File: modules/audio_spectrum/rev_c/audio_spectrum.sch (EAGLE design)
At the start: 97 parts, among them J1 MODULE_GENERIC_DEBUG, J2 AUDIO-JACK-VERTICAL, J7 TC2030-JLINK-L, P1 4k-200k, P2 4k-200k, Q1 NX3008PBK, Q2 NX3008PBK, U1 AT45DB641EUDFN, U2 MSGEQ7, U3 MSGEQ7, U5 OPA344, U6 OPA344, U7 TLV62130, U8 MP23AB02B, X1 16MHz

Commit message: added amplifier for sam4l adc, routed pcb
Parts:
- added C31, C32: 1.2nF, passives:CAPACITOR0603_CAP
- added R28, R31: 1.5k, passives:RESISTOR0603_RES
- added R29, R30: 19k, passives:RESISTOR0603_RES
- added U4, U9: OPA344, SparkFun-AnalogIC:OPA344
- renumbered U$1 to U100
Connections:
- removed net N$31: U100.PA06
- new net N$24: TP8.TESTPOINT, U100.PB01
- new net N$26: C31.2, R28.2, R29.1, U4.-IN
- new net N$8: C32.2, R30.1, R31.2, U9.-IN
- new net N87: C6.1, C7.2, P2.W, R17.2, R31.1, TP10.TESTPOINT, U6.OUT
- new net N90: C5.1, C8.2, P1.W, R14.2, R28.1, TP9.TESTPOINT, U5.OUT
- net !FLASH_CS: now also U1.!CS, U100.PA15; no longer U100.PB06
- net !FLASH_RESET: now also U1.!RESET
- net 3V3: now also U1.!WP, U1.VCC
- net ADC_IN_EXTRN: now also C32.1, R30.2, U9.OUT; no longer C6.1, C7.2, P2.W, R17.2, TP10.TESTPOINT, U6.OUT
- net ADC_IN_MEMS: now also C31.1, R29.2, U4.OUT; no longer C5.1, C8.2, P1.W, R14.2, TP9.TESTPOINT, U5.OUT
- net DBG_RX: now also U100.PA11; no longer U100.PB01
- net DBG_TX: now also U100.PA12; no longer U100.PB00
- net FLASH_SCLK: now also U1.SCK
- net FLASH_SI: now also U1.SI
- net FLASH_SO: now also U1.SO
- net GND: now also U1.GND, U4.+IN, U4.V-, U9.+IN, U9.V-
- net LEDG1: now also U100.PB06; no longer U100.PA16
- net LEDG2: now also U100.PB04; no longer U100.PA14
- net LEDR1: now also U100.PB07; no longer U100.PA17
- net LEDR2: now also U100.PB05; no longer U100.PA15
- net N$22: now also TP7.TESTPOINT, U100.PB00; no longer U1.!WP
- net SPEC2_GATED: now also U9.V+
- net SPEC2_STROBE: now also U100.PA06; no longer U100.PA09
- net SPEC_GATED: now also U4.V+
- net SPEC_POWER: no longer TP8.TESTPOINT, U100.PA12
- net SPEC_RESET: no longer TP7.TESTPOINT, U100.PA11
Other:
- note removed: "Controller"
- moved on the sheet: C11, C12, C13, C14, C21, C22, C23, C25, C26, C29, C3, C30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

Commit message: added digikey part attribute for all parts
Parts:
- C10: DIGIKEY (none) -> 490-1503-1-ND
- C11, C12, C14, C15: DIGIKEY (none) -> 490-1532-1-ND
- C21, C22, C23: DIGIKEY (none) -> 490-1536-1-ND
- C25, C26: DIGIKEY (none) -> 490-3297-1-ND
- C27: DIGIKEY (none) -> 490-6405-1-ND
- C28: DIGIKEY (none) -> 490-13241-1-ND
- C29, C30: DIGIKEY (none) -> 490-1440-1-ND
- C3, C4: DIGIKEY (none) -> 490-1415-1-ND
- C31, C32: DIGIKEY (none) -> 490-1304-1-ND
- C5, C6: DIGIKEY (none) -> 490-1427-1-ND
- C7, C8, C9: DIGIKEY (none) -> 490-1494-1-ND
- LED1, LED3: DIGIKEY (none) -> 160-1446-1-ND
- LED2, LED4: DIGIKEY (none) -> 160-1447-1-ND
- R10, R11, R12, R13: DIGIKEY (none) -> RHM20KCGCT-ND
- R14: DIGIKEY (none) -> RHM60.4KCLCT-ND
- R17, R18, R23, R24: DIGIKEY (none) -> RHM100KCGCT-ND
- R19, R20: DIGIKEY (none) -> RHM200KCFCT-ND
- R21: DIGIKEY (none) -> RHM240KCFCT-ND
- R22: DIGIKEY (none) -> RHM750KCFCT-ND
- R26, R27, R8, R9: DIGIKEY (none) -> RHM10.0KHCT-ND
- R28, R31, R5, R6: DIGIKEY (none) -> RHM1.5KCGCT-ND
- R29, R30: DIGIKEY (none) -> RHM19.1KCFCT-ND
- U4, U5, U6, U9: DIGIKEY (none) -> OPA344NACT-ND

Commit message: update to fix comments
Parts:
- removed TP11, TP12, TP13, TP14, TP15, TP16: TEST_POINT_0.040IN, headers:TEST_POINT_0.040IN
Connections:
- net GND: no longer TP11.TESTPOINT
- net MOD_IN: no longer TP14.TESTPOINT
- net MOD_OUT: no longer TP15.TESTPOINT
- net PPS: no longer TP16.TESTPOINT
- net SCL: no longer TP12.TESTPOINT
- net SDA: no longer TP13.TESTPOINT
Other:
- note added: "Gain set to 12.59 (22dB) matches MSGEQ7 22 dB internal amp"

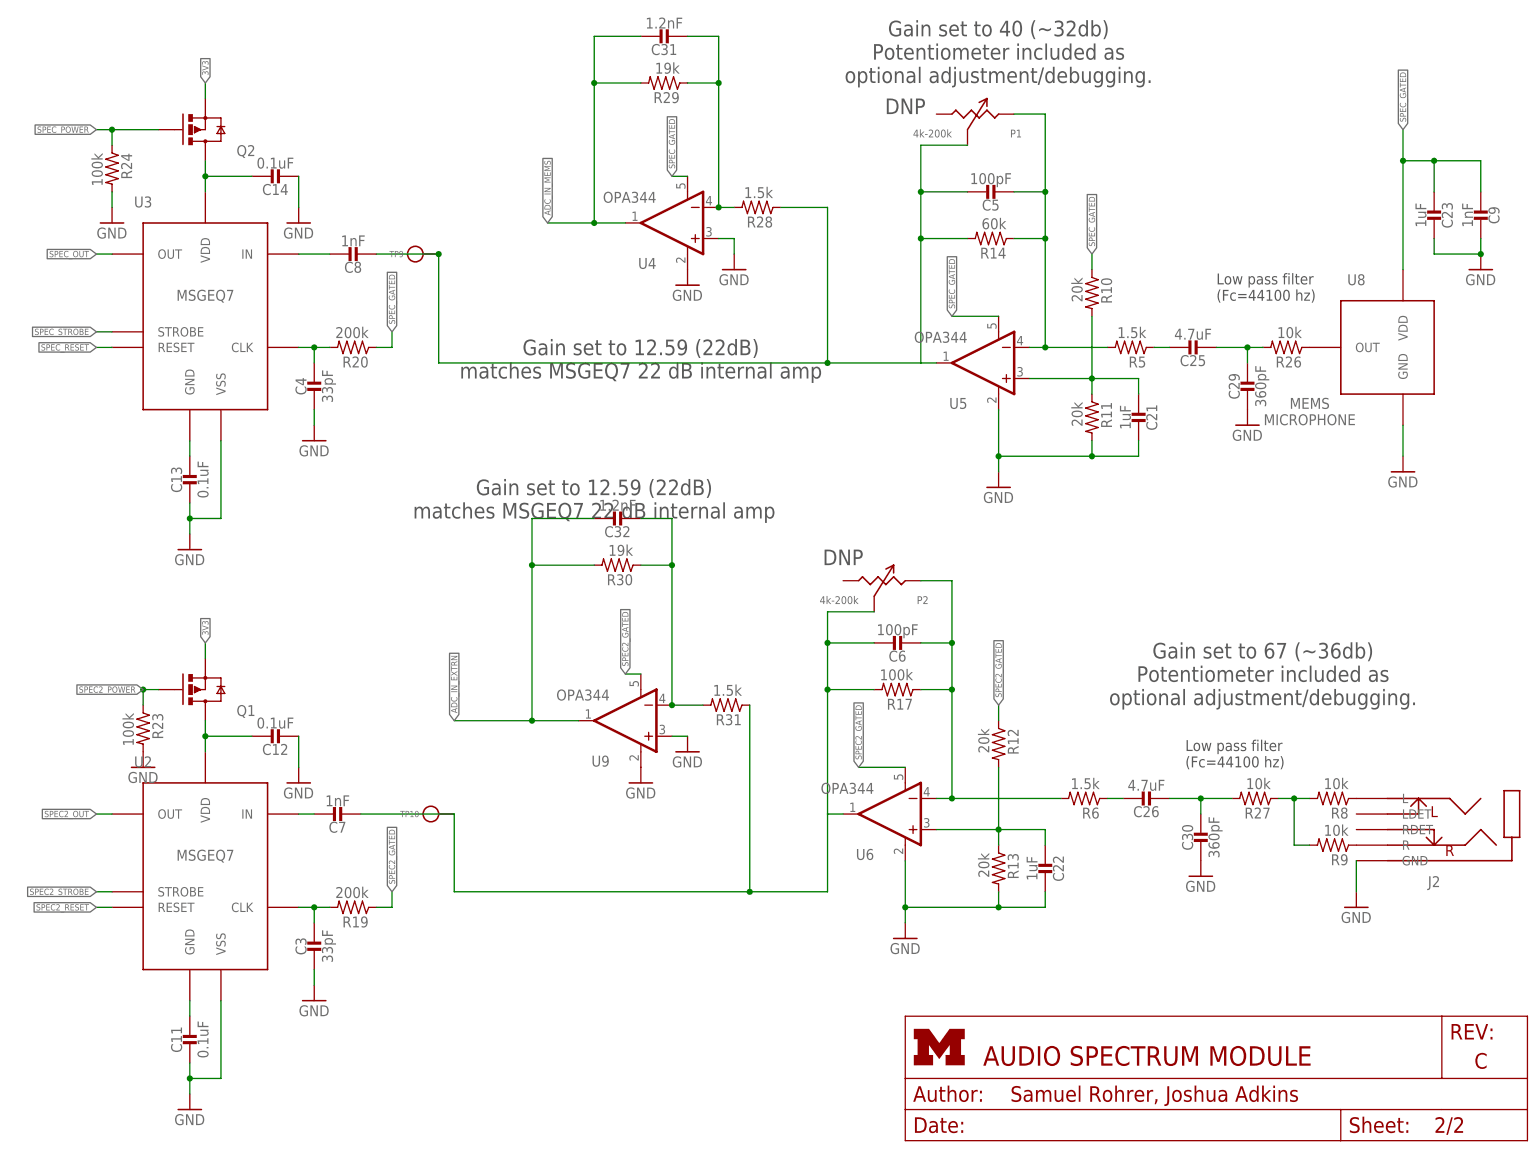
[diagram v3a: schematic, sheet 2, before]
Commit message: finish audio board, generated gerbers and BOM
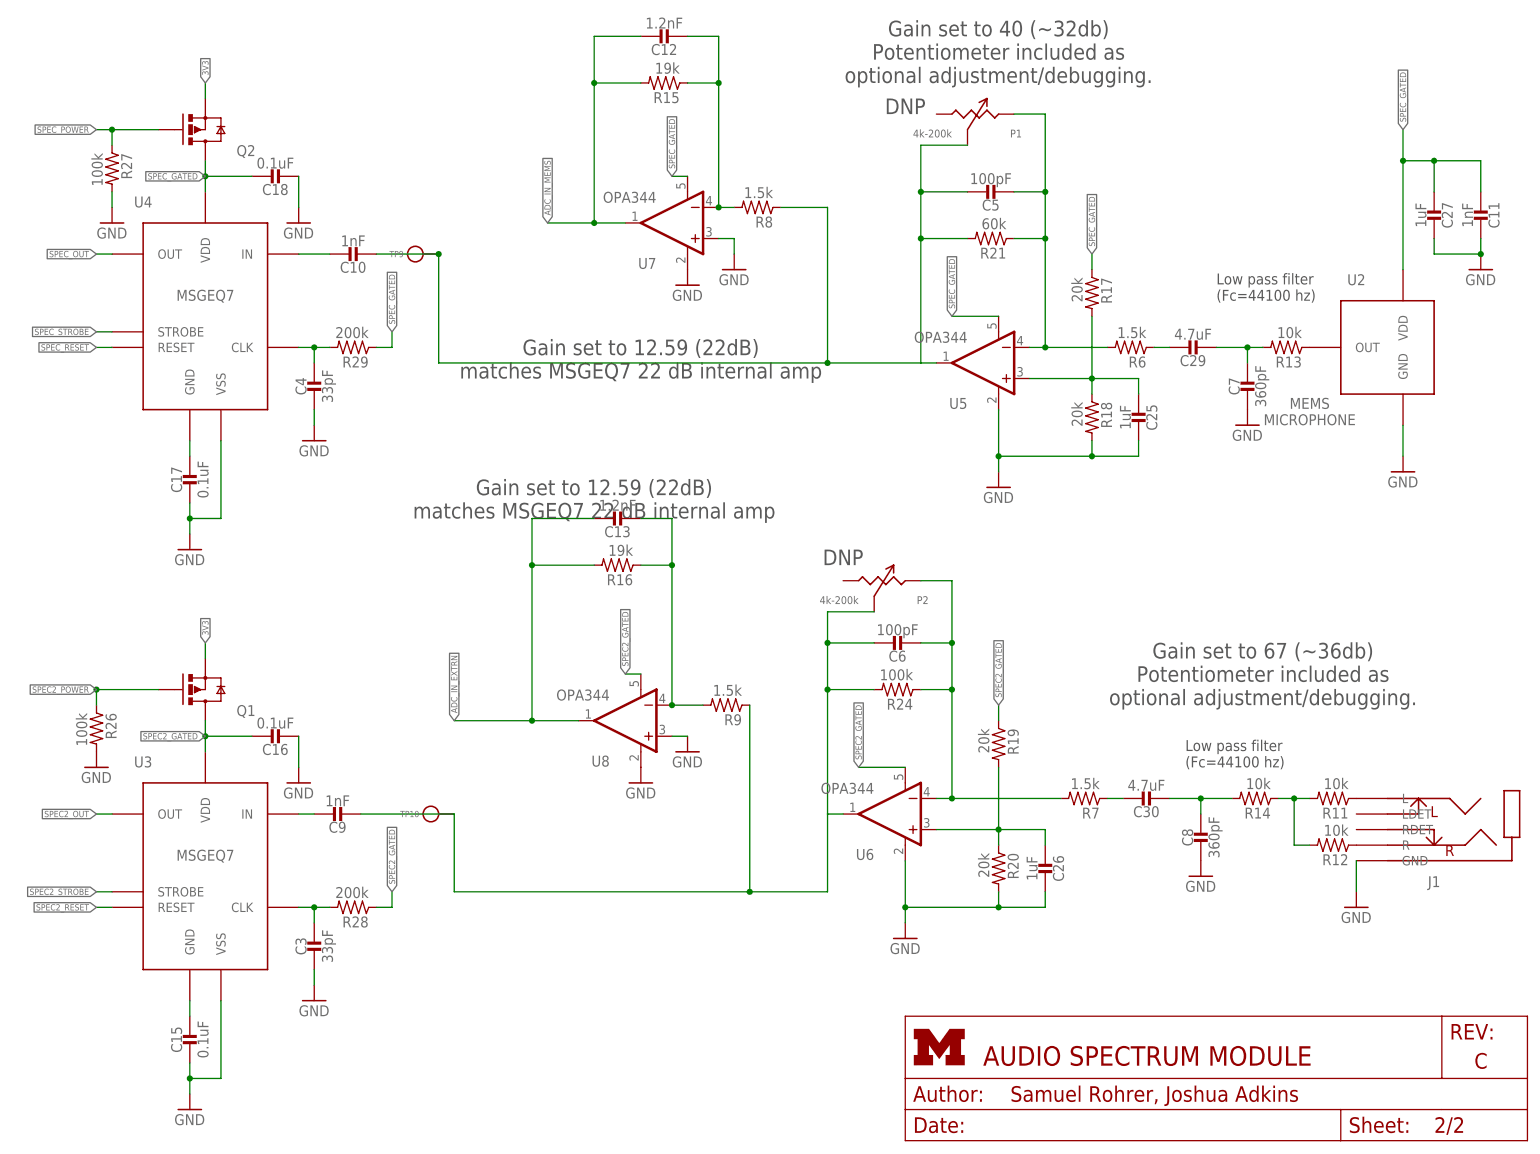
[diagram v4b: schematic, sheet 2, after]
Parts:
- removed U100: SAM4LC8BA, chips:SAM4LC8BA
- added U10: TLV62130, chips:TLV62130
- C1, C2: DIGIKEY 490-8230-1-ND -> 478-1215-1-ND
- C10: value 3.3nF -> 1nF; DIGIKEY 490-1503-1-ND -> 490-1494-1-ND
- C11: value 0.1uF -> 1nF; DIGIKEY 490-1532-1-ND -> 490-1494-1-ND
- C12: value 0.1uF -> 1.2nF; DIGIKEY 490-1532-1-ND -> 490-13298-1-ND
- C13: value 0.1uF -> 1.2nF; DIGIKEY (none) -> 490-13298-1-ND
- C14: value 0.1uF -> 3.3nF; DIGIKEY 490-1532-1-ND -> 490-1503-1-ND
- C16, C17, C18, C19: value 100nF -> 0.1uF; DIGIKEY 490-10777-1-ND -> 490-1532-1-ND
- C20: device passives:CAPACITOR0402_CAP -> passives:CAPACITOR0603_CAP; DIGIKEY 490-10777-1-ND -> 490-1532-1-ND
- C21, C22, C23: value 1uF -> 100nF; DIGIKEY 490-1536-1-ND -> 490-1532-1-ND
- C24: value 4.7uF -> 100nF; DIGIKEY 490-13252-1-ND -> 490-10777-1-ND
- C25, C26: value 4.7uF -> 1uF; DIGIKEY 490-3297-1-ND -> 490-1536-1-ND
- C27: value 10uF -> 1uF; DIGIKEY 490-6405-1-ND -> 490-1536-1-ND
- C28: value 22uF -> 4.7uF; device passives:CAPACITOR0603_CAP -> passives:CAPACITOR0402_CAP; DIGIKEY 490-13241-1-ND -> 490-13252-1-ND
- C29, C30: value 360pF -> 4.7uF; DIGIKEY 490-1440-1-ND -> 490-3297-1-ND
- C31: value 1.2nF -> 10uF; DIGIKEY 490-1304-1-ND -> 490-6405-1-ND
- C32: value 1.2nF -> 22uF; DIGIKEY 490-1304-1-ND -> 490-13241-1-ND
- C7, C8: value 1nF -> 360pF; DIGIKEY 490-1494-1-ND -> 490-1440-1-ND
- J1: value MODULE_GENERIC_DEBUG -> AUDIO-JACK-VERTICAL; device signpost:MODULE_GENERIC_DEBUG -> connector:AUDIO-JACK-VERTICAL
- J2: value AUDIO-JACK-VERTICAL -> MODULE_GENERIC_DEBUG; device connector:AUDIO-JACK-VERTICAL -> signpost:MODULE_GENERIC_DEBUG
- R1: value 1k -> 0
- R10, R11, R12, R13: value 20k -> 10k; DIGIKEY RHM20KCGCT-ND -> RHM10.0KHCT-ND
- R14: value 60k -> 10k; DIGIKEY RHM60.4KCLCT-ND -> RHM10.0KHCT-ND
- R15, R16: value 100k -> 19k; DIGIKEY 1276-3432-1-ND -> RHM19.1KCFCT-ND
- R17, R18: value 100k -> 20k; DIGIKEY RHM100KCGCT-ND -> RHM20KCGCT-ND
- R19, R20: value 200k -> 20k; DIGIKEY RHM200KCFCT-ND -> RHM20KCGCT-ND
- R2: DIGIKEY 1276-3431-1-ND -> RHM1.0KDCT-N
- R21: value 240k -> 60k; DIGIKEY RHM240KCFCT-ND -> RHM60.4KCLCT-ND
- R22: value 750k -> 100k; DIGIKEY RHM750KCFCT-ND -> RHM100KCGCT-ND
- R25: value 0 -> 100k; DIGIKEY 1276-3431-1-ND -> RHM100KCGCT-ND
- R26, R27: value 10k -> 100k; DIGIKEY RHM10.0KHCT-ND -> RHM100KCGCT-ND
- R28: value 1.5k -> 200k; DIGIKEY RHM1.5KCGCT-ND -> RHM200KCFCT-ND
- R29: value 19k -> 200k; DIGIKEY RHM19.1KCFCT-ND -> RHM200KCFCT-ND
- R3, R4: DIGIKEY 1276-3431-1-ND -> RHM1.0KDCT-ND
- R30: value 19k -> 240k; DIGIKEY RHM19.1KCFCT-ND -> RHM240KCFCT-ND
- R31: value 1.5k -> 750k; DIGIKEY RHM1.5KCGCT-ND -> RHM750KCFCT-ND
- R5: value 1.5k -> 1k; DIGIKEY RHM1.5KCGCT-ND -> RHM1.0KDCT-ND
- R7: value 10k -> 1.5k; DIGIKEY 1276-3431-1-ND -> RHM1.5KCGCT-ND
- R8, R9: value 10k -> 1.5k; DIGIKEY RHM10.0KHCT-ND -> RHM1.5KCGCT-ND
- U2: value MSGEQ7 -> MP23AB02B; device chips:MSGEQ7 -> chips:MP23AB02B
- U4: value OPA344 -> MSGEQ7; device SparkFun-AnalogIC:OPA344 -> chips:MSGEQ7; DIGIKEY OPA344NACT-ND -> (none)
- U7: value TLV62130 -> OPA344; device chips:TLV62130 -> SparkFun-AnalogIC:OPA344; DIGIKEY (none) -> OPA344NACT-ND
- U8: value MP23AB02B -> OPA344; device chips:MP23AB02B -> SparkFun-AnalogIC:OPA344; DIGIKEY (none) -> OPA344NACT-ND
- U9: value OPA344 -> SAM4LC8BA; device SparkFun-AnalogIC:OPA344 -> chips:SAM4LC8BA; DIGIKEY OPA344NACT-ND -> (none)
- renumbered J7 to J3
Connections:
- net !AUDIO_RESET: now also J2.DBG_!RESET, U9.!RESET; no longer J1.DBG_!RESET, U100.!RESET
- net !FLASH_CS: now also U9.PA15; no longer U100.PA15
- net !FLASH_RESET: now also U9.PB11; no longer U100.PB11
- net 3V3: now also C21.1, C22.1, C23.1, C32.2, J2.VCCIO, R10.2, R23.2, R25.2, R31.2, U10.VOS, U9.VDDIN, U9.VDDIO, U9.VLCD, U9.VLCDIN; no longer C17.1, C18.1, C19.1, C28.2, J1.VCCIO, R15.2, R16.2, R18.2, R7.2, U100.VDDIN, U100.VDDIO, U100.VLCD, U100.VLCDIN, U7.VOS
- net 3VSWOUT: now also U10.SW; no longer U7.SW
- net 5V: now also C19.1, C31.1, J2.5V, U10.AVIN, U10.EN, U10.PVIN; no longer C15.1, C27.1, J1.5V, U7.AVIN, U7.EN, U7.PVIN
- net ADC_IN_EXTRN: now also C13.1, R16.2, U8.OUT, U9.PB03; no longer C32.1, R30.2, U100.PB03, U9.OUT
- net ADC_IN_MEMS: now also C12.1, R15.2, U7.OUT, U9.PB02; no longer C31.1, R29.2, U100.PB02, U4.OUT
- net AUDIO_SWDCLK: now also J2.DBG_SWDCLK, R23.1, U9.TCK; no longer J1.DBG_SWDCLK, R16.1, U100.TCK
- net AUDIO_SWDIO: now also J2.DBG_SWDIO, R22.1, U9.PA03; no longer J1.DBG_SWDIO, R15.1, U100.PA03
- net AUDIO_XIN: now also U9.PA00; no longer U100.PA00
- net AUDIO_XOUT: now also U9.PA01; no longer U100.PA01
- net CONTROLLER_BUCK/LDO_N: now also R1.2, R10.1, U9.PA02; no longer R25.2, R7.1, U100.PA02
- net DBG_GPIO1: now also J2.DBG_GPIO1, U9.PB14; no longer J1.DBG_GPIO1, U100.PB14
- net DBG_GPIO2: now also J2.DBG_GPIO2, U9.PB15; no longer J1.DBG_GPIO2, U100.PB15
- net DBG_RX: now also J2.DBG_RX, U9.PA11; no longer J1.DBG_RX, U100.PA11
- net DBG_TX: now also J2.DBG_TX, U9.PA12; no longer J1.DBG_TX, U100.PA12
- net FLASH_SCLK: now also U9.PB08; no longer U100.PB08
- net FLASH_SI: now also U9.PB09; no longer U100.PB09
- net FLASH_SO: now also U9.PB10; no longer U100.PB10
- net GND: now also C11.1, C14.1, C21.2, C22.2, C23.2, C25.1, C26.1, C27.1, C28.2, C31.2, C32.1, C7.2, C8.2, R1.1, R18.2, R20.2, R26.2, R27.2, R30.1, U10.AGND, U10.DEF, U10.FSW, U10.PGND, U2.GND, U4.VSS, U7.+IN, U7.V-, U8.+IN, U8.V-, U9.GND, U9.GNDANA; no longer C10.1, C11.2, C12.2, C13.2, C14.2, C21.1, C22.1, C23.1, C27.2, C28.1, C29.2, C30.2, C9.1, R11.2, R13.2, R21.1, R23.2, R24.2, R25.1, U100.GND, U100.GNDANA, U2.VSS, U4.+IN, U4.V-, U7.AGND, U7.DEF, U7.FSW, U7.PGND, U8.GND, U9.+IN, U9.V-
- net LEDG1: now also R2.1, U9.PB06; no longer R1.1, U100.PB06
- net LEDG2: now also R4.1, U9.PB04; no longer R3.1, U100.PB04
- net LEDR1: now also R3.1, U9.PB07; no longer R2.1, U100.PB07
- net LEDR2: now also R5.1, U9.PB05; no longer R4.1, U100.PB05
- net MOD_IN: now also J2.MOD_IN, U9.PA20; no longer J1.MOD_IN, U100.PA20
- net MOD_OUT: now also J2.MOD_OUT, U9.PA19; no longer J1.MOD_OUT, U100.PA19
- net N$1: now also C15.1, U3.GND; no longer C11.1, U2.GND
- net N$10: now also R11.2, R12.2, R14.1; no longer R27.1, R8.2, R9.2
- net N$11: now also C26.2, R19.2, R20.1; no longer C22.2, R12.2, R13.1
- net N$12: now also R21.1, R6.2; no longer R14.1, R5.2
- net N$13: now also C29.1, R6.1; no longer C25.1, R5.1
- net N$14: now also R24.1, R7.2; no longer R17.1, R6.2
- net N$15: now also C30.1, R7.1; no longer C26.1, R6.1
- net N$16: now also J1.R, R12.1; no longer J2.R, R9.1
- net N$17: now also J1.L, R11.1; no longer J2.L, R8.1
- net N$18: now also R13.1, U2.OUT; no longer R26.1, U8.OUT
- net N$19: now also C17.1, U4.GND; no longer C13.1, U3.GND
- net N$2: now also R28.2, U3.CLK; no longer R19.2, U2.CLK
- net N$20: now also C30.2, C8.1, R14.2; no longer C26.2, C30.1, R27.2
- net N$21: now also R2.2; no longer R1.2
- net N$22: now also U9.PB00; no longer U100.PB00
- net N$23: now also R3.2; no longer R2.2
- net N$24: now also U9.PB01; no longer U100.PB01
- net N$25: now also R5.2; no longer R4.2
- net N$26: now also C12.2, R15.1, R8.2, U7.-IN; no longer C31.2, R28.2, R29.1, U4.-IN
- net N$3: now also C9.1, U3.IN; no longer C7.1, U2.IN
- net N$32: now also C20.1, U9.VDDANA; no longer C16.1, U100.VDDANA
- net N$33: now also R4.2; no longer R3.2
- net N$34: now also C14.2, U10.SS/TR; no longer C10.2, U7.SS/TR
- net N$36: now also R25.1, U10.PG; no longer R18.1, U7.PG
- net N$37: now also R30.2, R31.1, U10.FB; no longer R21.2, R22.1, U7.FB
- net N$4: now also U9.VDDCORE; no longer U100.VDDCORE
- net N$44: now also C28.1, U9.VDDOUT; no longer C20.1, U100.VDDOUT
- net N$5: now also C29.2, C7.1, R13.2; no longer C25.2, C29.1, R26.2
- net N$53: now also U9.BIASH, U9.BIASL; no longer U100.BIASH, U100.BIASL
- net N$54: now also U9.CAPH, U9.CAPL; no longer U100.CAPH, U100.CAPL
- net N$6: now also R29.2, U4.CLK; no longer R20.2, U3.CLK
- net N$7: now also C10.1, U4.IN; no longer C8.1, U3.IN
- net N$8: now also C13.2, R16.1, R9.2, U8.-IN; no longer C32.2, R30.1, R31.2, U9.-IN
- net N$9: now also C25.2, R17.2, R18.1; no longer C21.2, R10.2, R11.1
- net N87: now also C9.2, R24.2, R9.1; no longer C7.2, R17.2, R31.1
- net N90: now also C10.2, R21.2, R8.1; no longer C8.2, R14.2, R28.1
- net PPS: now also J2.PPS, U9.PA18; no longer J1.PPS, U100.PA18
- net SCL: now also J2.SCL, U9.PA24; no longer J1.SCL, U100.PA24
- net SDA: now also J2.SDA, U9.PA23; no longer J1.SDA, U100.PA23
- net SPEC2_GATED: now also C16.1, R28.1, U3.VDD, U8.V+; no longer C12.1, R12.1, U2.VDD, U9.V+
- net SPEC2_OUT: now also U3.OUT, U9.PA05; no longer U100.PA05, U2.OUT
- net SPEC2_POWER: now also R26.1, U9.PA08; no longer R23.1, U100.PA08
- net SPEC2_RESET: now also U3.RESET, U9.PA07; no longer U100.PA07, U2.RESET
- net SPEC2_STROBE: now also U3.STROBE, U9.PA06; no longer U100.PA06, U2.STROBE
- net SPEC_GATED: now also C11.2, C18.1, C27.2, R17.1, R29.1, U2.VDD, U4.VDD, U7.V+; no longer C14.1, C23.2, C9.2, R10.1, R20.1, U3.VDD, U4.V+, U8.VDD
- net SPEC_OUT: now also U4.OUT, U9.PA04; no longer U100.PA04, U3.OUT
- net SPEC_POWER: now also R27.1; no longer R24.1
- net SPEC_RESET: now also U4.RESET; no longer U3.RESET
- net SPEC_STROBE: now also U4.STROBE, U9.PA10; no longer U100.PA10, U3.STROBE
- net USB+: now also J2.USB_D+, U9.PA26; no longer J1.USB_D+, U100.PA26
- net USB-: now also J2.USB_D-, U9.PA25; no longer J1.USB_D-, U100.PA25
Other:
- moved on the sheet: C11, C12, C13, C19, C20, C24, C25, C26, C28, C29, C30, C7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
